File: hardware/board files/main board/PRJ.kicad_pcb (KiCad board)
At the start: 2 copper layers, 30 x 29.2 mm, 24 parts, among them J1 Strain Gauge, J2 Programmer, J3 KLIPPER, U1 HX717, U2 ATtiny202-SS, U3 AMS1117-3.3

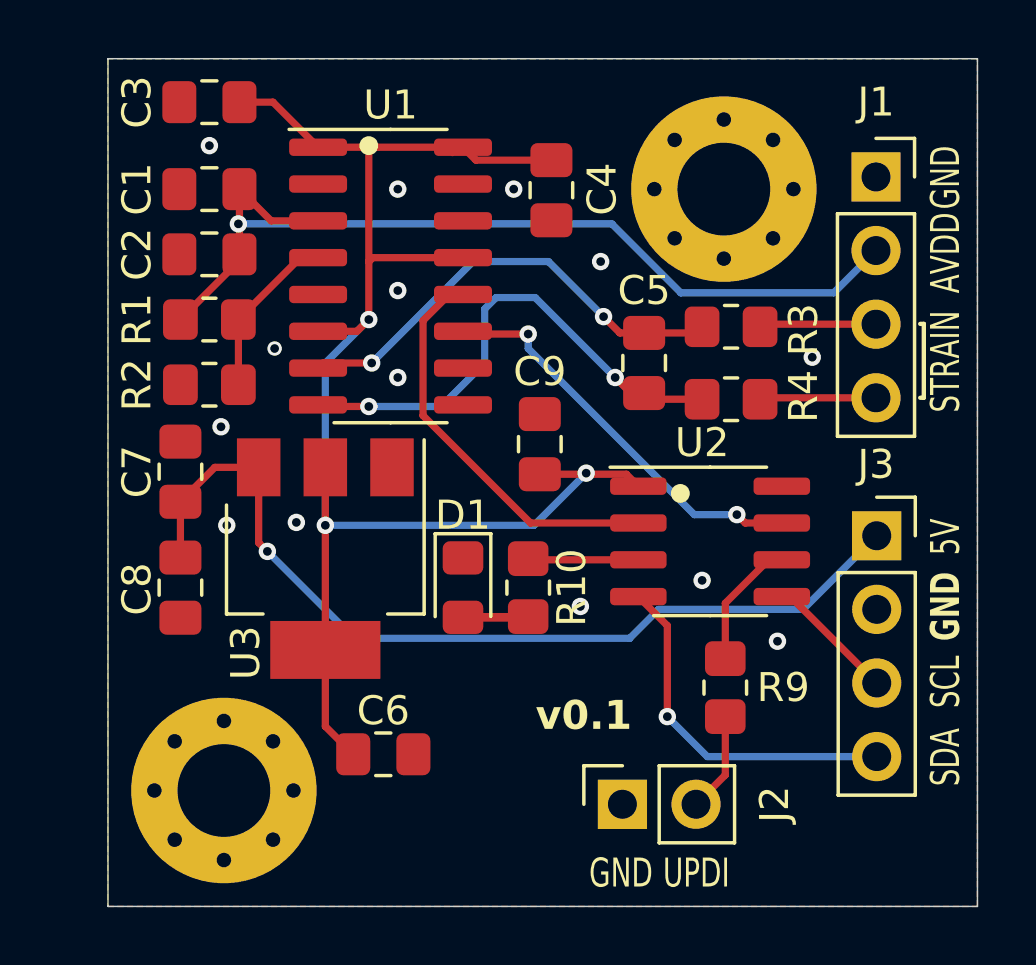
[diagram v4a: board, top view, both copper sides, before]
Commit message: added initial prototype of production unit with attiny202 and hx71708
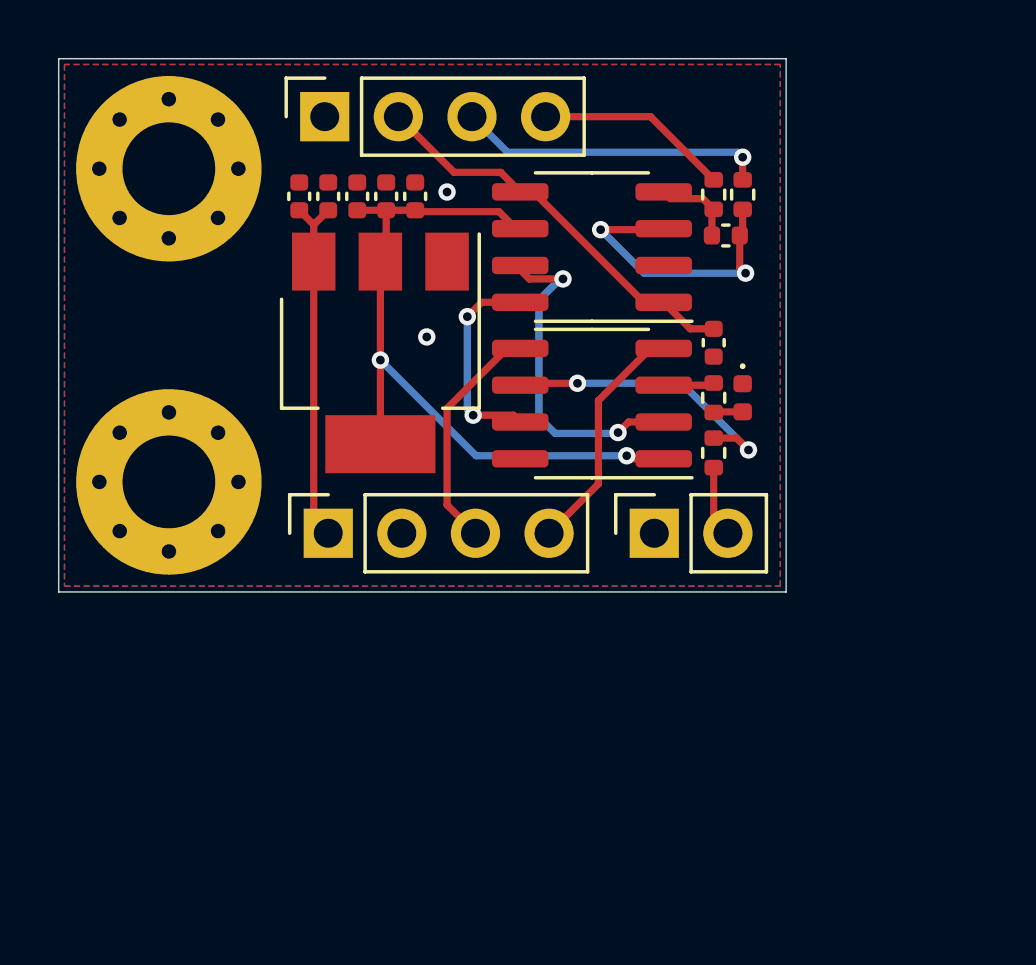
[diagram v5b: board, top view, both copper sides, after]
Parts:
- removed C3: 0u1, Capacitor_SMD:C_0805_2012Metric_Pad1.18x1.45mm_HandSolder
- removed C8: 10u, Capacitor_SMD:C_0805_2012Metric_Pad1.18x1.45mm_HandSolder
- removed R10: 100, Resistor_SMD:R_0805_2012Metric_Pad1.20x1.40mm_HandSolder
- removed R9: 4k7, Resistor_SMD:R_0805_2012Metric_Pad1.20x1.40mm_HandSolder
- C1, C4: footprint Capacitor_SMD:C_0805_2012Metric_Pad1.18x1.45mm_HandSolder -> Capacitor_SMD:C_0402_1005Metric
- C2, C7, C9: value 10u -> 0u1; footprint Capacitor_SMD:C_0805_2012Metric_Pad1.18x1.45mm_HandSolder -> Capacitor_SMD:C_0402_1005Metric
- C5, C6: value 0u1 -> 10u; footprint Capacitor_SMD:C_0805_2012Metric_Pad1.18x1.45mm_HandSolder -> Capacitor_SMD:C_0402_1005Metric
- D1: footprint LED_SMD:LED_0805_2012Metric_Pad1.15x1.40mm_HandSolder -> LED_SMD:LED_0402_1005Metric
- R1: value 33K -> 100; footprint Resistor_SMD:R_0805_2012Metric_Pad1.20x1.40mm_HandSolder -> Resistor_SMD:R_0402_1005Metric
- R2: value 12K -> 100; footprint Resistor_SMD:R_0805_2012Metric_Pad1.20x1.40mm_HandSolder -> Resistor_SMD:R_0402_1005Metric
- R3: value 100 -> 4k7; footprint Resistor_SMD:R_0805_2012Metric_Pad1.20x1.40mm_HandSolder -> Resistor_SMD:R_0402_1005Metric
- R4: footprint Resistor_SMD:R_0805_2012Metric_Pad1.20x1.40mm_HandSolder -> Resistor_SMD:R_0402_1005Metric
- U1: value HX717 -> HX71708; footprint Package_SO:SOP-16_3.9x9.9mm_P1.27mm -> Package_SO:SOIC-8_3.9x4.9mm_P1.27mm
- moved H2 21.6 mm to (106.6, 102.1)
- moved H1 21.5 mm to (106.6, 91.3)
- moved C6 19.3 mm to (113.1, 92.2), turned to 90 degrees
- moved J1 19.1 mm to (112.0, 89.5), turned to 90 degrees
- moved J3 18.9 mm to (112.1, 103.9), turned to 90 degrees
- moved R1 18.9 mm to (126.4, 92.2), turned to -90 degrees
- moved R2 18.6 mm to (125.4, 92.2), turned to -90 degrees
- moved C2 17.7 mm to (125.4, 97.3), turned to -90 degrees
- moved C5 13.2 mm to (111.1, 92.2)
- moved C7 12.5 mm to (115.1, 92.2)
- moved D1 11.7 mm to (126.4, 99.2)
- moved C9 9.65 mm to (125.8, 93.6), turned to 0 degrees
- moved J2 9.41 mm to (123.3, 103.9)
- moved C4 7.70 mm to (112.1, 92.2)
- moved U3 7.35 mm to (113.9, 97.7)
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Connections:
- C1 pad 1: AVDD -> GND
- C1 pad 2: GND -> +3.3V
- C4 pad 1: GND -> +5V
- C4 pad 2: +3.3V -> GND
- C5 pad 1: IN+ -> +5V
- C5 pad 2: IN- -> GND
- C7 pad 1: +5V -> +3.3V
- C9 pad 1: +3.3V -> IN+
- C9 pad 2: GND -> IN-
- R1 pad 1: AVDD -> Net-(J1-Pin_3)
- R1 pad 2: Net-(U1-VFB) -> IN-
- R2 pad 1: Net-(U1-VFB) -> Net-(J1-Pin_4)
- R2 pad 2: GND -> IN+
- R3 pad 1: Net-(J1-Pin_3) -> Net-(U2-~{RESET}/PA0)
- R3 pad 2: IN- -> UPDI
- R4 pad 1: Net-(J1-Pin_4) -> Net-(U2-PA7)
- R4 pad 2: IN+ -> Net-(D1-A)
- U1 pad 1: +3.3V -> AVDD
- U1 pad 3: AVDD -> IN-
- U1 pad 4: Net-(U1-VFB) -> IN+
- U1 pad 5: GND -> AVDD
- U1 pad 7: IN- -> DOUT
- U1 pad 8: IN+ -> PD_SCK
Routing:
- net +3.3V: track 55.3 -> 25.1 mm, vias 3 -> 2
- net +5V: track 31.9 -> 12.3 mm, vias 1 -> 0
- net AVDD: track 32.2 -> 13.9 mm, vias 1 -> 0
- net IN+: track 17.7 -> 2.90 mm, vias 2 -> 0
- net PD_SCK: track 14.0 -> 7.09 mm
- net Net-(J1-Pin_3): track 4.04 -> 10.7 mm, vias 0 -> 1
- net Net-(U1-VFB): track 5.88 -> 0.00 mm
- net IN-: track 15.9 -> 10.1 mm
- net Net-(U2-~{RESET}/PA0): track 4.48 -> 10.2 mm, vias 0 -> 2
- net SDA: track 12.4 -> 8.28 mm, vias 1 -> 0
- net SCL: track 4.51 -> 8.10 mm
- net Net-(J1-Pin_4): track 4.02 -> 6.70 mm
- net DOUT: track 14.0 -> 11.7 mm, vias 0 -> 2
- net Net-(U2-PA7): track 3.82 -> 1.76 mm
- net Net-(D1-A): track 2.30 -> 1.01 mm
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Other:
- board size 30 x 29.2 mm -> 25.1 x 18.4 mm
- board text removed: "5V"
- board text removed: "AVDD"
- board text removed: "GND"
- board text removed: "SCL"
- board text removed: "SDA"
- board text removed: "STRAIN"
- board text removed: "UPDI"
- board text removed: "v0.1"
